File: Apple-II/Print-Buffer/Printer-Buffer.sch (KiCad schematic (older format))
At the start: 12 parts, among them J1 Apple-II-Expansion-Slot, J2 CONN_13X2, U1 HM6116, U2 74LS374, U3 74125, U4 74121, U5 74LS138, U6 74LS02, U7 7404

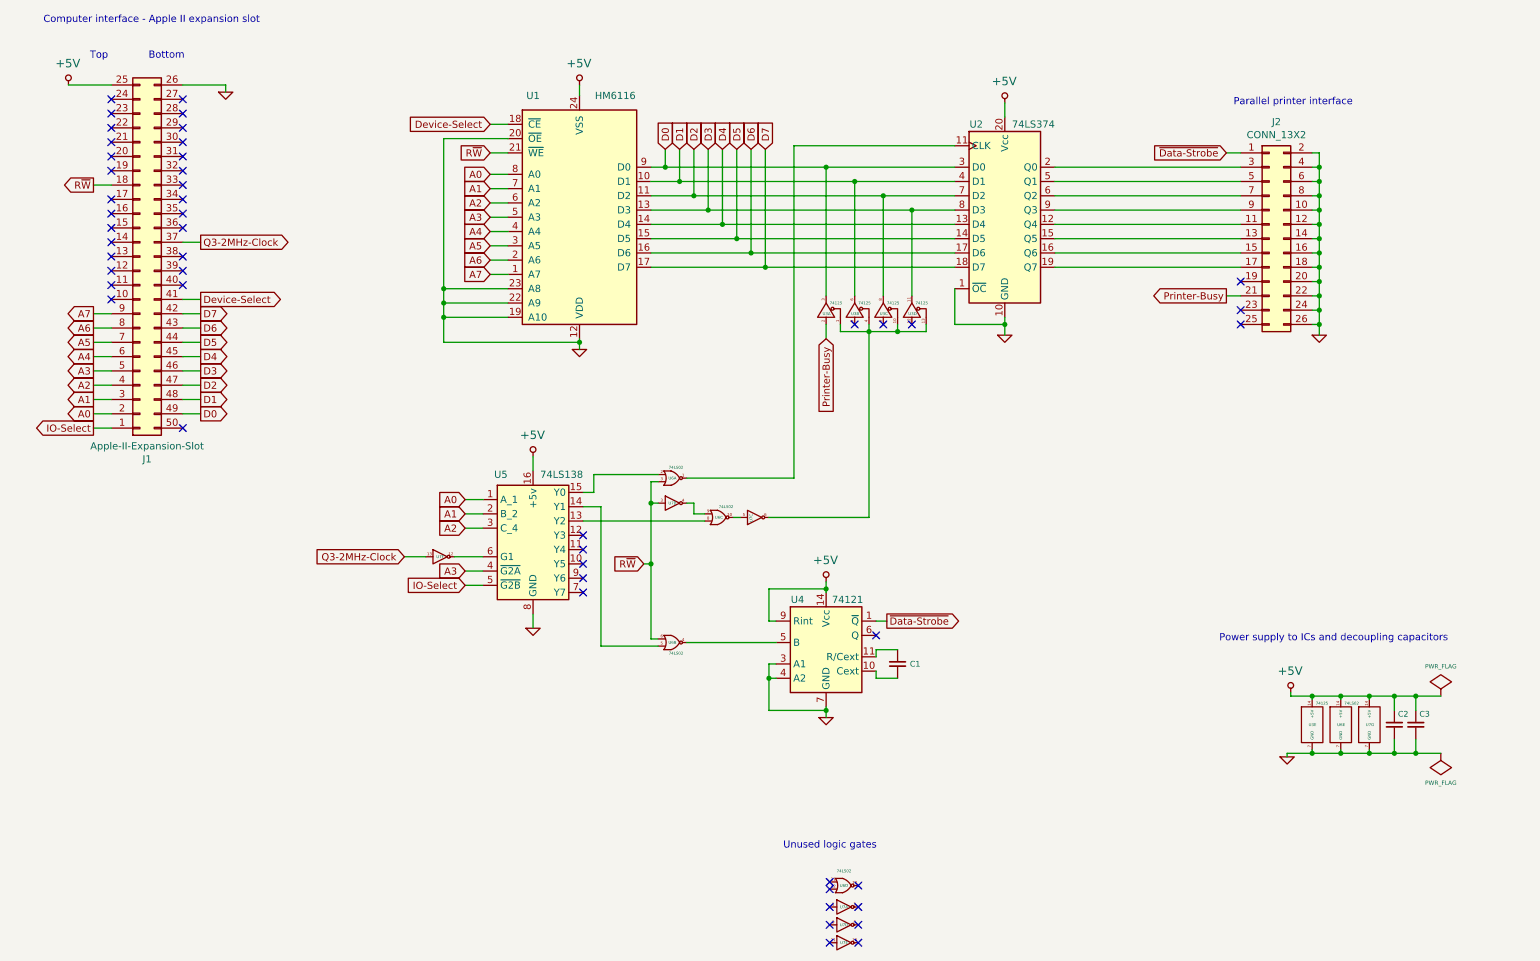
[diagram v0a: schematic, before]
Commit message: netlist and footprints
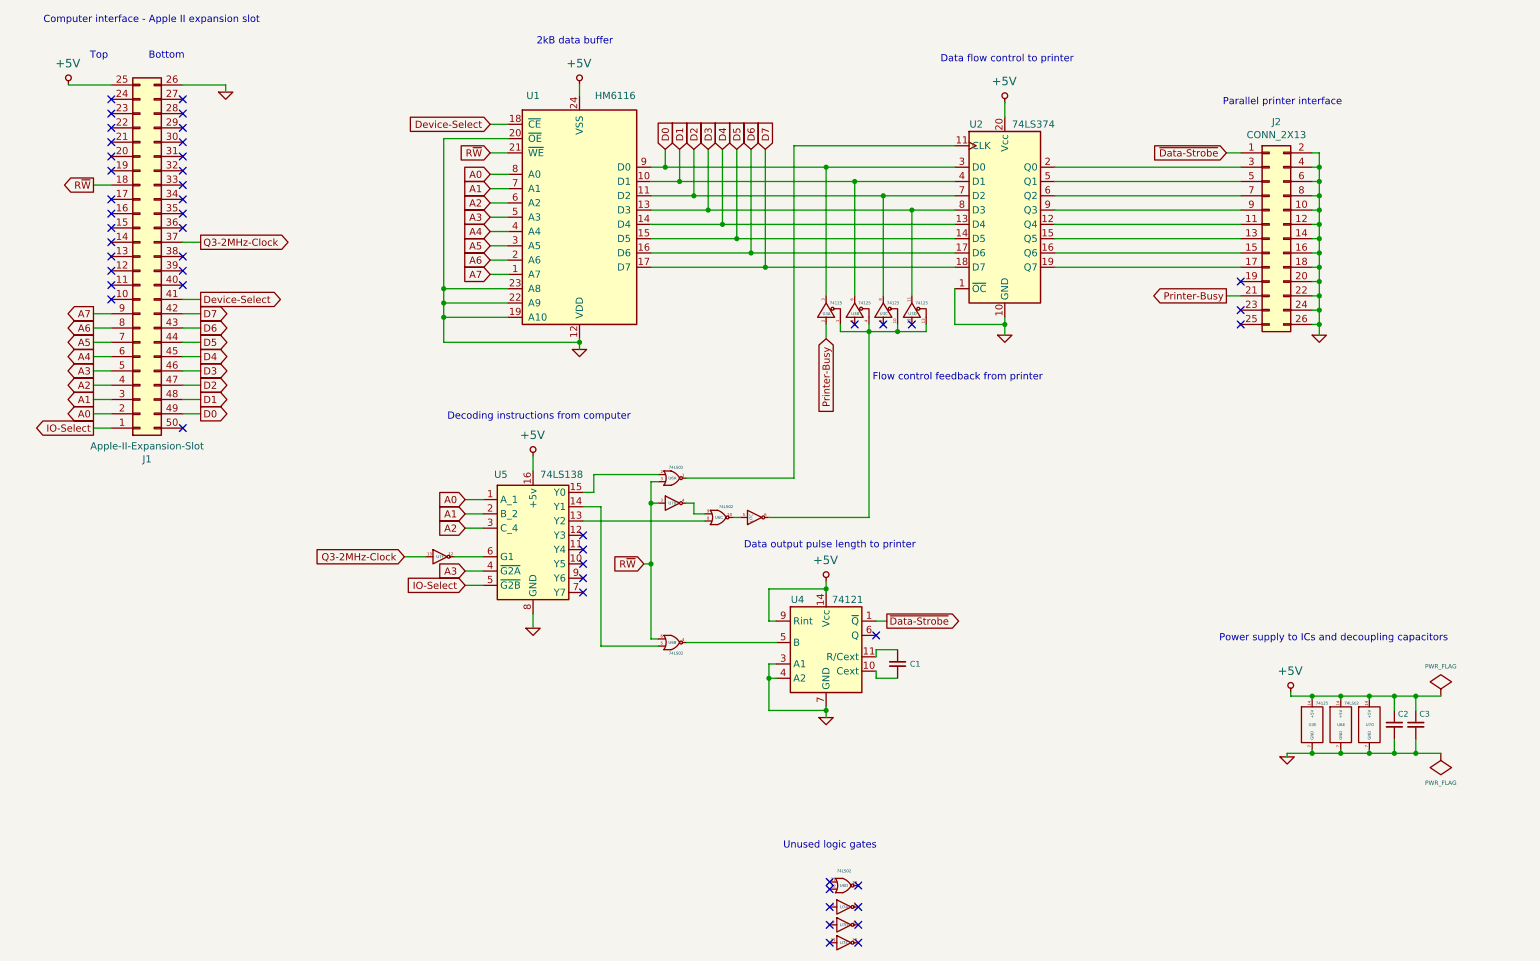
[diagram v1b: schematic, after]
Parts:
- C1, C2, C3: footprint (none) -> Print-Buffer:C_Rect_L7.0mm_W2.0mm_P5.00mm
- J1: footprint (none) -> Print-Buffer:Connector_2x25_P1.27mm_Polarized_Edge
- J2: value CONN_13X2 -> CONN_2X13; footprint (none) -> Print-Buffer:IDC-Header_2x13_P2.54mm_Vertical_Lock
- U1: footprint Package_DIP:DIP-40_W15.24mm -> Print-Buffer:DIP-24_W15.24mm
- U2: footprint (none) -> Print-Buffer:DIP-20_W7.62mm
- U3, U4, U6, U7: footprint (none) -> Print-Buffer:DIP-14_W7.62mm
- U5: footprint (none) -> Print-Buffer:DIP-16_W7.62mm
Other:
- note added: "2kB data buffer"
- note added: "Data flow control to printer"
- note added: "Data output pulse length to printer"
- note added: "Decoding instructions from computer"
- note added: "Flow control feedback from printer"
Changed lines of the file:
@@
 F 0 "U1" H 4375 3375 50  0000 C CNN
 F 1 "HM6116" H 4950 3375 50  0000 C CNN
-F 2 "Package_DIP:DIP-40_W15.24mm" H 4750 1325 50  0001 C CNN
+F 2 "Print-Buffer:DIP-24_W15.24mm" H 4750 1325 50  0001 C CNN
 F 3 "" H 4700 2425 50  0001 C CNN
 	1    4700 2525
@@
 F 0 "J1" H 1675 4217 50  0000 C CNN
 F 1 "Apple-II-Expansion-Slot" H 1675 4126 50  0000 C CNN
-F 2 "" H 1625 3500 50  0001 C CNN
+F 2 "Print-Buffer:Connector_2x25_P1.27mm_Polarized_Edge" H 1625 3500 50  0001 C CNN
 F 3 "" H 1625 3500 50  0001 C CNN
 	1    1675 2800
@@
 F 0 "U5" H 4150 5275 50  0000 C CNN
 F 1 "74LS138" H 4575 5275 50  0000 C CNN
-F 2 "" H 4375 4850 60  0000 C CNN
+F 2 "Print-Buffer:DIP-16_W7.62mm" H 4375 4850 60  0001 C CNN
 F 3 "" H 4375 4850 60  0000 C CNN
 	1    4375 4800
@@
 F 0 "U3" V 6400 3150 20  0000 L CNN
 F 1 "74125" V 6475 3200 20  0000 L CNN
-F 2 "" H 6475 3175 60  0000 C CNN
+F 2 "Print-Buffer:DIP-14_W7.62mm" H 6475 3175 60  0001 C CNN
 F 3 "" H 6475 3175 60  0000 C CNN
 	1    6425 3175
@@
 F 0 "U3" V 6600 3150 20  0000 L CNN
 F 1 "74125" V 6675 3200 20  0000 L CNN
-F 2 "" H 6675 3175 60  0000 C CNN
+F 2 "Print-Buffer:DIP-14_W7.62mm" H 6675 3175 60  0001 C CNN
 F 3 "" H 6675 3175 60  0000 C CNN
 	2    6625 3175
@@
 F 0 "U3" V 6800 3150 20  0000 L CNN
 F 1 "74125" V 6875 3200 20  0000 L CNN
-F 2 "" H 6875 3175 60  0000 C CNN
+F 2 "Print-Buffer:DIP-14_W7.62mm" H 6875 3175 60  0001 C CNN
 F 3 "" H 6875 3175 60  0000 C CNN
 	3    6825 3175
@@
 F 0 "U3" V 7000 3150 20  0000 L CNN
 F 1 "74125" V 7075 3200 20  0000 L CNN
-F 2 "" H 7075 3175 60  0000 C CNN
+F 2 "Print-Buffer:DIP-14_W7.62mm" H 7075 3175 60  0001 C CNN
 F 3 "" H 7075 3175 60  0000 C CNN
 	4    7025 3175
@@
 F 0 "U6" H 5350 4350 20  0000 C CNN
 F 1 "74LS02" H 5375 4425 20  0000 C CNN
-F 2 "" H 5400 4350 60  0000 C CNN
+F 2 "Print-Buffer:DIP-14_W7.62mm" H 5400 4350 60  0001 C CNN
 F 3 "" H 5400 4350 60  0000 C CNN
 	1    5350 4350
@@
 F 0 "U6" H 5350 5500 20  0000 C CNN
 F 1 "74LS02" H 5375 5575 20  0000 C CNN
-F 2 "" H 5400 5500 60  0000 C CNN
+F 2 "Print-Buffer:DIP-14_W7.62mm" H 5400 5500 60  0001 C CNN
 F 3 "" H 5400 5500 60  0000 C CNN
 	2    5350 5500
@@
 F 0 "U7" H 3725 4900 20  0000 C CNN
 F 1 "7404" H 3725 5000 20  0001 C CNN
-F 2 "" H 3775 4900 60  0000 C CNN
+F 2 "Print-Buffer:DIP-14_W7.62mm" H 3775 4900 60  0001 C CNN
 F 3 "" H 3775 4900 60  0000 C CNN
 	6    3725 4900
@@
 P 9575 2675
 F 0 "J2" H 9575 3492 50  0000 C CNN
-F 1 "CONN_13X2" H 9575 3401 50  0000 C CNN
-F 2 "" H 9525 2775 50  0001 C CNN
+F 1 "CONN_2X13" H 9575 3401 50  0000 C CNN
+F 2 "Print-Buffer:IDC-Header_2x13_P2.54mm_Vertical_Lock" H 9525 2775 50  0001 C CNN
 F 3 "" H 9525 2775 50  0001 C CNN
 	1    9575 2675
@@
 F 0 "U2" H 7475 3175 50  0000 C CNN
 F 1 "74LS374" H 7875 3175 50  0000 C CNN
-F 2 "" H 7675 2775 60  0000 C CNN
+F 2 "Print-Buffer:DIP-20_W7.62mm" H 7675 2775 60  0001 C CNN
 F 3 "" H 7675 2775 60  0000 C CNN
 	1    7675 2525
@@
 F 0 "U3" H 9800 6075 20  0000 L CNN
 F 1 "74125" H 9850 6225 20  0000 L CNN
-F 2 "" H 9875 6075 60  0000 C CNN
+F 2 "Print-Buffer:DIP-14_W7.62mm" H 9875 6075 60  0001 C CNN
 F 3 "" H 9875 6075 60  0000 C CNN
 	5    9825 6075
@@
 F 0 "U7" V 5900 4600 20  0000 L CNN
 F 1 "7404" H 5925 4725 20  0001 C CNN
-F 2 "" H 5975 4625 60  0000 C CNN
+F 2 "Print-Buffer:DIP-14_W7.62mm" H 5975 4625 60  0001 C CNN
 F 3 "" H 5975 4625 60  0000 C CNN
 	3    5925 4625
@@
 F 0 "C1" H 7011 5650 40  0000 L CNN
 F 1 "C" H 6975 5600 40  0001 L CNN
-F 2 "" H 6963 5500 30  0000 C CNN
+F 2 "Print-Buffer:C_Rect_L7.0mm_W2.0mm_P5.00mm" H 6963 5500 30  0001 C CNN
 F 3 "" H 6925 5650 60  0000 C CNN
 	1    6925 5650
@@
 F 0 "U6" H 5675 4625 20  0000 C CNN
 F 1 "74LS02" H 5725 4550 20  0000 C CNN
-F 2 "" H 5725 4625 60  0000 C CNN
+F 2 "Print-Buffer:DIP-14_W7.62mm" H 5725 4625 60  0001 C CNN
 F 3 "" H 5725 4625 60  0000 C CNN
 	3    5675 4625
@@
 F 0 "U6" H 10000 6075 20  0000 L CNN
 F 1 "74LS02" H 10050 6225 20  0000 L CNN
-F 2 "" H 10075 6075 60  0000 C CNN
+F 2 "Print-Buffer:DIP-14_W7.62mm" H 10075 6075 60  0001 C CNN
 F 3 "" H 10075 6075 60  0000 C CNN
 	5    10025 6075
@@
 F 0 "U6" H 6550 7200 20  0000 C CNN
 F 1 "74LS02" H 6550 7302 20  0000 C CNN
-F 2 "" H 6600 7200 60  0000 C CNN
+F 2 "Print-Buffer:DIP-14_W7.62mm" H 6600 7200 60  0001 C CNN
 F 3 "" H 6600 7200 60  0000 C CNN
 	4    6550 7200
@@
 F 0 "U7" H 6550 7350 20  0000 C CNN
 F 1 "7404" H 6550 7450 20  0001 C CNN
-F 2 "" H 6600 7350 60  0000 C CNN
+F 2 "Print-Buffer:DIP-14_W7.62mm" H 6600 7350 60  0001 C CNN
 F 3 "" H 6600 7350 60  0000 C CNN
 	1    6550 7350
@@
 F 0 "U7" H 10200 6075 20  0000 L CNN
 F 1 "7404" H 10225 6175 20  0001 C CNN
-F 2 "" H 10275 6075 60  0000 C CNN
+F 2 "Print-Buffer:DIP-14_W7.62mm" H 10275 6075 60  0001 C CNN
 F 3 "" H 10275 6075 60  0000 C CNN
 	7    10225 6075
@@
 F 0 "U7" H 6550 7475 20  0000 C CNN
 F 1 "7404" H 6550 7575 20  0001 C CNN
-F 2 "" H 6600 7475 60  0000 C CNN
+F 2 "Print-Buffer:DIP-14_W7.62mm" H 6600 7475 60  0001 C CNN
 F 3 "" H 6600 7475 60  0000 C CNN
 	4    6550 7475
@@
 F 0 "U7" H 6550 7600 20  0000 C CNN
 F 1 "7404" H 6550 7700 20  0001 C CNN
-F 2 "" H 6600 7600 60  0000 C CNN
+F 2 "Print-Buffer:DIP-14_W7.62mm" H 6600 7600 60  0001 C CNN
 F 3 "" H 6600 7600 60  0000 C CNN
 	5    6550 7600
@@
 F 0 "C2" H 10425 6150 40  0000 L CNN
 F 1 "C" H 10450 6025 40  0001 L CNN
-F 2 "" H 10438 5925 30  0000 C CNN
+F 2 "Print-Buffer:C_Rect_L7.0mm_W2.0mm_P5.00mm" H 10438 5925 30  0001 C CNN
 F 3 "" H 10400 6075 60  0000 C CNN
 	1    10400 6075
@@
 F 0 "C3" H 10575 6150 40  0000 L CNN
 F 1 "C" H 10600 6025 40  0001 L CNN
-F 2 "" H 10588 5925 30  0000 C CNN
+F 2 "Print-Buffer:C_Rect_L7.0mm_W2.0mm_P5.00mm" H 10588 5925 30  0001 C CNN
 F 3 "" H 10550 6075 60  0000 C CNN
 	1    10550 6075
@@
 F 0 "U4" H 6225 5900 50  0000 C CNN
 F 1 "74121" H 6575 5900 50  0000 C CNN
-F 2 "" H 6425 5500 60  0000 C CNN
+F 2 "Print-Buffer:DIP-14_W7.62mm" H 6425 5500 60  0001 C CNN
 F 3 "" H 6425 5500 60  0000 C CNN
 	1    6425 5550
@@
 F 0 "U7" H 5350 4525 20  0000 C CNN
 F 1 "7404" H 5350 4625 20  0001 C CNN
-F 2 "" H 5400 4525 60  0000 C CNN
+F 2 "Print-Buffer:DIP-14_W7.62mm" H 5400 4525 60  0001 C CNN
 F 3 "" H 5400 4525 60  0000 C CNN
 	2    5350 4525
@@
 Text Notes 950  1175 0    50   ~ 0
 Computer interface - Apple II expansion slot
-Text Notes 9275 1750 0    50   ~ 0
+Text Notes 9200 1750 0    50   ~ 0
 Parallel printer interface
+Text Notes 4400 1325 0    50   ~ 0
+2kB data buffer
+Text Notes 7225 1450 0    50   ~ 0
+Data flow control to printer
+Text Notes 3775 3950 0    50   ~ 0
+Decoding instructions from computer
+Text Notes 5850 4850 0    50   ~ 0
+Data output pulse length to printer
+Text Notes 6750 3675 0    50   ~ 0
+Flow control feedback from printer
 $EndSCHEMATC

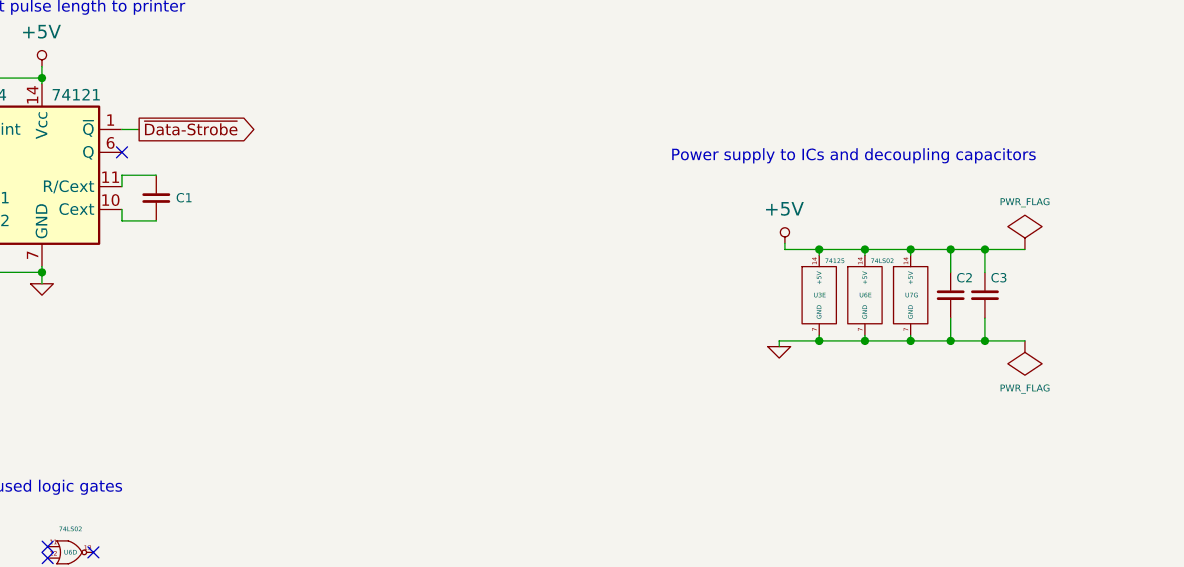
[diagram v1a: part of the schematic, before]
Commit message: show values for caps and resistors
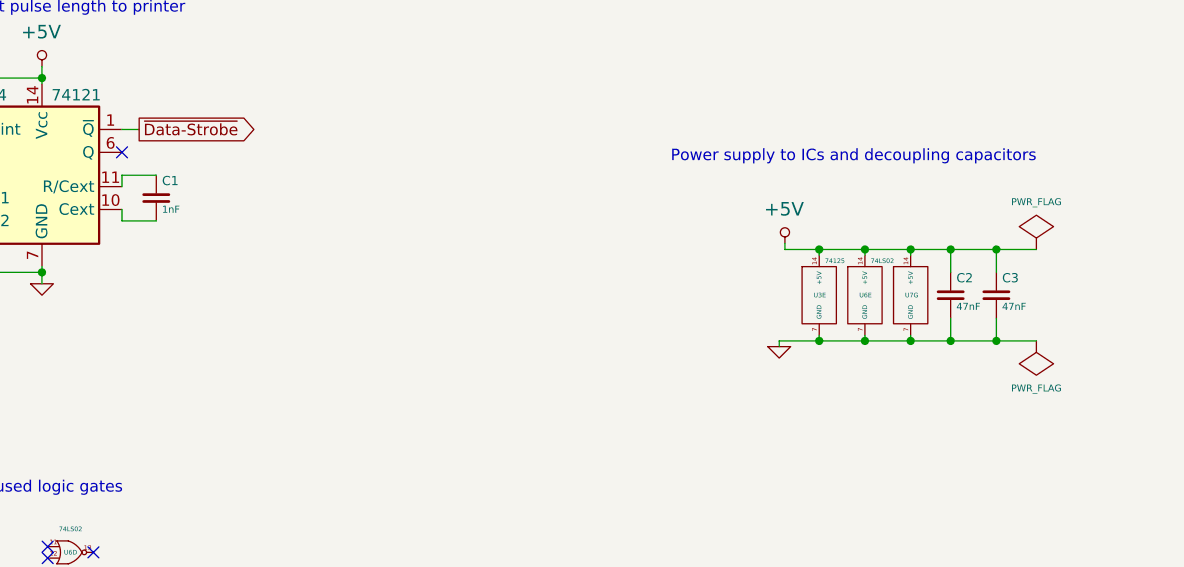
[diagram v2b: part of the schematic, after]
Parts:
- C1: value C -> 1nF
- C2, C3: value C -> 47nF
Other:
- moved on the sheet: C3
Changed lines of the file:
@@
 L Printer-Buffer:PWR_FLAG #FLG0101
 U 1 1 655569C4
-P 10725 5875
-F 0 "#FLG0101" H 10725 5970 30  0001 C CNN
-F 1 "PWR_FLAG" H 10725 6083 30  0000 C CNN
-F 2 "" H 10725 5875 60  0000 C CNN
-F 3 "" H 10725 5875 60  0000 C CNN
-	1    10725 5875
+P 10775 5875
+F 0 "#FLG0101" H 10775 5970 30  0001 C CNN
+F 1 "PWR_FLAG" H 10775 6083 30  0000 C CNN
+F 2 "" H 10775 5875 60  0000 C CNN
+F 3 "" H 10775 5875 60  0000 C CNN
+	1    10775 5875
 	1    0    0    -1
 $EndComp
@@
 L Printer-Buffer:PWR_FLAG #FLG0102
 U 1 1 655569F2
-P 10725 6275
-F 0 "#FLG0102" H 10725 6370 30  0001 C CNN
-F 1 "PWR_FLAG" H 10725 6482 30  0000 C CNN
-F 2 "" H 10725 6275 60  0000 C CNN
-F 3 "" H 10725 6275 60  0000 C CNN
-	1    10725 6275
+P 10775 6275
+F 0 "#FLG0102" H 10775 6370 30  0001 C CNN
+F 1 "PWR_FLAG" H 10775 6482 30  0000 C CNN
+F 2 "" H 10775 6275 60  0000 C CNN
+F 3 "" H 10775 6275 60  0000 C CNN
+	1    10775 6275
 	-1   0    0    1
 $EndComp
@@
 U 1 1 6561A2B7
 P 6925 5650
-F 0 "C1" H 7011 5650 40  0000 L CNN
-F 1 "C" H 6975 5600 40  0001 L CNN
+F 0 "C1" H 6950 5725 40  0000 L CNN
+F 1 "1nF" H 6950 5600 31  0000 L CNN
 F 2 "Print-Buffer:C_Rect_L7.0mm_W2.0mm_P5.00mm" H 6963 5500 30  0001 C CNN
 F 3 "" H 6925 5650 60  0000 C CNN
@@
 P 10400 6075
 F 0 "C2" H 10425 6150 40  0000 L CNN
-F 1 "C" H 10450 6025 40  0001 L CNN
+F 1 "47nF" H 10425 6025 31  0000 L CNN
 F 2 "Print-Buffer:C_Rect_L7.0mm_W2.0mm_P5.00mm" H 10438 5925 30  0001 C CNN
 F 3 "" H 10400 6075 60  0000 C CNN
@@
 Connection ~ 10400 5875
 Wire Wire Line
-	10400 5875 10550 5875
+	10400 5875 10600 5875
 Wire Wire Line
 	10400 6175 10400 6275
 Connection ~ 10400 6275
 Wire Wire Line
-	10400 6275 10550 6275
+	10400 6275 10600 6275
 $Comp
 L Printer-Buffer:C C3
 U 1 1 653E6A6A
-P 10550 6075
-F 0 "C3" H 10575 6150 40  0000 L CNN
-F 1 "C" H 10600 6025 40  0001 L CNN
-F 2 "Print-Buffer:C_Rect_L7.0mm_W2.0mm_P5.00mm" H 10588 5925 30  0001 C CNN
-F 3 "" H 10550 6075 60  0000 C CNN
-	1    10550 6075
-	1    0    0    -1
-$EndComp
-Wire Wire Line
-	10550 5975 10550 5875
-Connection ~ 10550 5875
-Wire Wire Line
-	10550 5875 10725 5875
-Wire Wire Line
-	10550 6175 10550 6275
-Connection ~ 10550 6275
-Wire Wire Line
-	10550 6275 10725 6275
+P 10600 6075
+F 0 "C3" H 10625 6150 40  0000 L CNN
+F 1 "47nF" H 10625 6025 31  0000 L CNN
+F 2 "Print-Buffer:C_Rect_L7.0mm_W2.0mm_P5.00mm" H 10638 5925 30  0001 C CNN
+F 3 "" H 10600 6075 60  0000 C CNN
+	1    10600 6075
+	1    0    0    -1
+$EndComp
+Wire Wire Line
+	10600 5975 10600 5875
+Connection ~ 10600 5875
+Wire Wire Line
+	10600 5875 10775 5875
+Wire Wire Line
+	10600 6175 10600 6275
+Connection ~ 10600 6275
+Wire Wire Line
+	10600 6275 10775 6275
 NoConn ~ 6450 7475
 NoConn ~ 6450 7600

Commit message: PCB layout
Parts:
- J2: value CONN_2X13 -> CONN_13X2
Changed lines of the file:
@@
-$EndComp
-$Comp
-L Printer-Buffer:CONN_13X2 J2
-U 1 1 6534E0E8
-P 9575 2675
-F 0 "J2" H 9575 3492 50  0000 C CNN
-F 1 "CONN_2X13" H 9575 3401 50  0000 C CNN
-F 2 "Print-Buffer:IDC-Header_2x13_P2.54mm_Vertical_Lock" H 9525 2775 50  0001 C CNN
-F 3 "" H 9525 2775 50  0001 C CNN
-	1    9575 2675
-	1    0    0    -1
 $EndComp
 $Comp
@@
 Text Notes 6750 3675 0    50   ~ 0
 Flow control feedback from printer
+$Comp
+L Printer-Buffer:CONN_13X2 J2
+U 1 1 653CD63A
+P 9575 2675
+F 0 "J2" H 9575 3492 50  0000 C CNN
+F 1 "CONN_13X2" H 9575 3401 50  0000 C CNN
+F 2 "Print-Buffer:IDC-Header_2x13_P2.54mm_Vertical_Lock" H 9525 2775 50  0001 C CNN
+F 3 "" H 9525 2775 50  0001 C CNN
+	1    9575 2675
+	1    0    0    -1
+$EndComp
 $EndSCHEMATC
